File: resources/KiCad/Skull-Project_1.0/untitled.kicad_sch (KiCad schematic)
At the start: 1 part

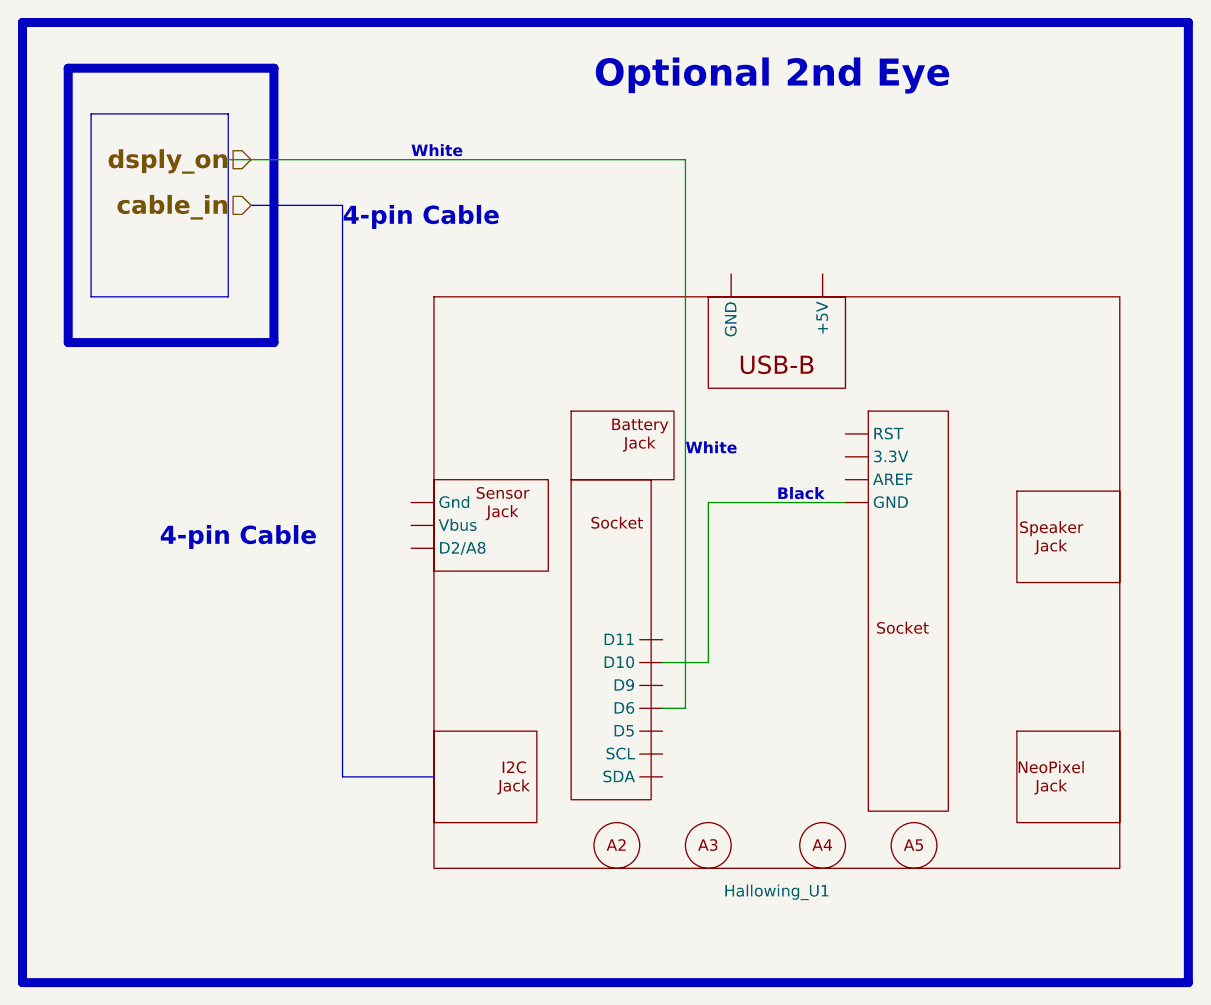
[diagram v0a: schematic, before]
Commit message: add rst-2-prim to schematic
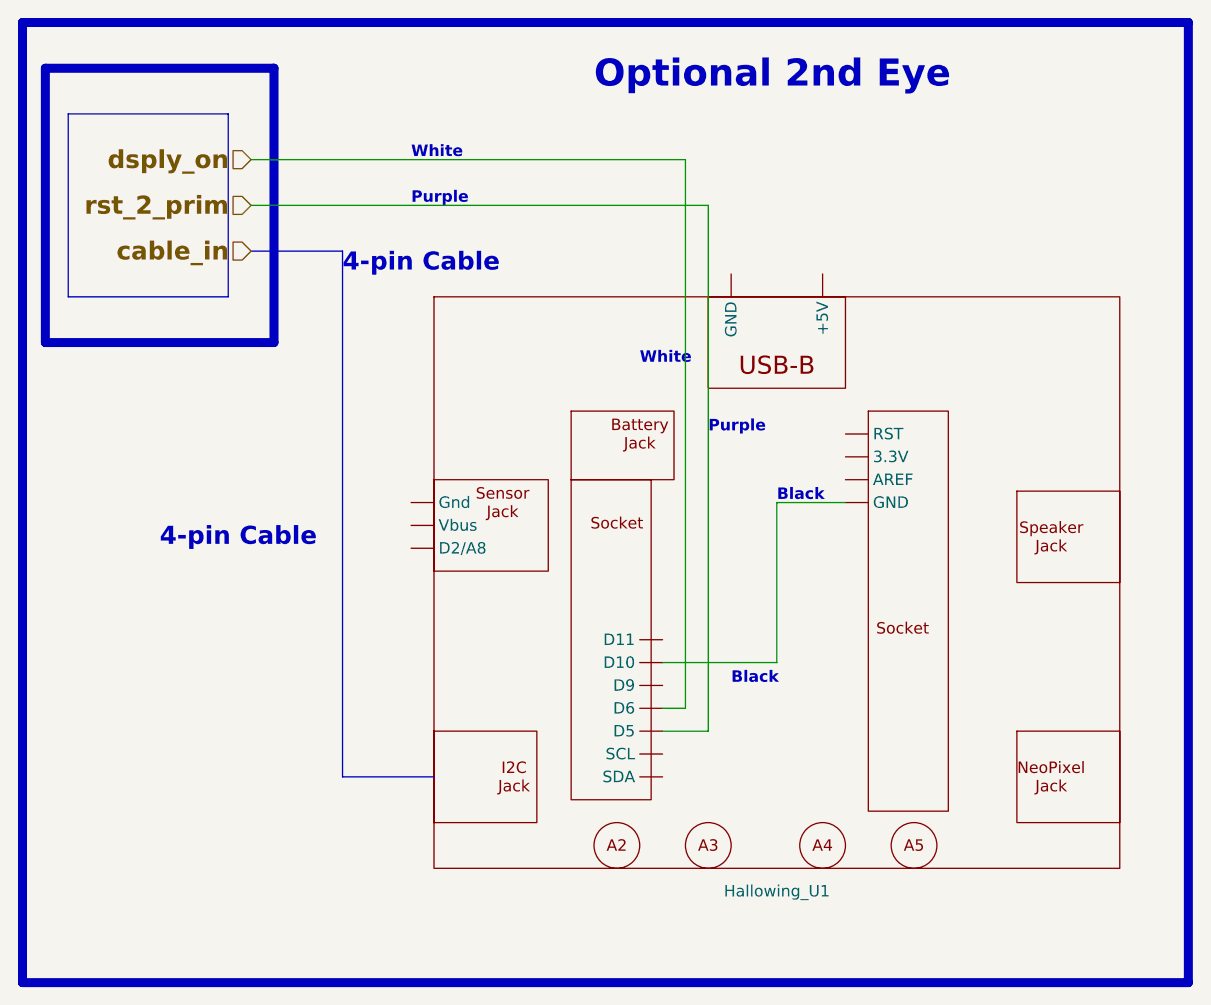
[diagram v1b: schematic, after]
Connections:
- net rst_2_prim : now reaches Hallowing_U1. (Vbus)
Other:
- note added: "Purple"
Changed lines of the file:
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@@
   (title_block
     (title "Skull-Project 1.0")
-    (date "2024-09-25")
+    (date "2024-09-27")
     (rev "1.0")
     (company "github.com/Mark-MDO47/Skull-Project")
     (comment 2 "NOTE: Hallowing as from display side (not connector side)")
   )
-  (wire (pts (xy 152.4 116.84) (xy 147.32 116.84))
+  (bus (pts (xy 101.6 71.12) (xy 111.76 71.12))
     (stroke (width 0) (type default))
   )
-  (bus (pts (xy 111.76 66.04) (xy 111.76 129.54))
+  (wire (pts (xy 101.6 60.96) (xy 149.86 60.96))
     (stroke (width 0) (type default))
   )
-  (wire (pts (xy 167.64 99.06) (xy 152.4 99.06))
+  (wire (pts (xy 147.32 116.84) (xy 160.02 116.84))
+    (stroke (width 0) (type default))
+  )
+  (wire (pts (xy 147.32 124.46) (xy 152.4 124.46))
+    (stroke (width 0) (type default))
+  )
+  (wire (pts (xy 167.64 99.06) (xy 160.02 99.06))
     (stroke (width 0) (type default))
   )
@@
     (stroke (width 0) (type default))
   )
-  (bus (pts (xy 101.6 66.04) (xy 111.76 66.04))
+  (wire (pts (xy 152.4 124.46) (xy 152.4 66.04))
+    (stroke (width 0) (type default))
+  )
+  (bus (pts (xy 111.76 71.12) (xy 111.76 129.54))
     (stroke (width 0) (type default))
   )
@@
     (stroke (width 0) (type default))
   )
-  (wire (pts (xy 99.06 60.96) (xy 149.86 60.96))
+  (wire (pts (xy 160.02 116.84) (xy 160.02 99.06))
     (stroke (width 0) (type default))
   )
-  (wire (pts (xy 152.4 99.06) (xy 152.4 116.84))
+  (wire (pts (xy 152.4 66.04) (xy 101.6 66.04))
     (stroke (width 0) (type default))
   )
@@
     (stroke (width 0) (type default))
   )
-  (rectangle (start 81.28 50.8) (end 104.14 81.28)
+  (rectangle (start 78.74 50.8) (end 104.14 81.28)
     (stroke (width 1) (type default) (color 255 153 0 1))
     (fill (type none))
   )
-  (rectangle (start 83.82 55.88) (end 99.06 76.2)
+  (rectangle (start 81.28 55.88) (end 99.06 76.2)
     (stroke (width 0) (type default))
     (fill (type none))
@@
     (fill (type none))
   )
+  (text "Black" (at 154.94 119.38 0)
+    (effects (font (size 1.27 1.27) bold) (justify left bottom))
+  )
   (text "Black" (at 160.02 99.06 0)
+    (effects (font (size 1.27 1.27) bold) (justify left bottom))
+  )
+  (text "Purple" (at 152.4 91.44 0)
     (effects (font (size 1.27 1.27) bold) (justify left bottom))
   )
@@
     (effects (font (size 1.27 1.27) bold) (justify left bottom))
   )
-  (text "4-pin Cable" (at 111.76 68.58 0)
+  (text "4-pin Cable" (at 111.76 73.66 0)
     (effects (font (size 2 2) bold) (justify left bottom))
+  )
+  (text "Purple" (at 119.38 66.04 0)
+    (effects (font (size 1.27 1.27) bold) (justify left bottom))
   )
   (text "4-pin Cable" (at 91.44 104.14 0)
@@
     (effects (font (size 3 3) (thickness 0.6) bold) (justify left bottom))
   )
-  (text "White" (at 149.86 93.98 0)
+  (text "White" (at 144.78 83.82 0)
     (effects (font (size 1.27 1.27) bold) (justify left bottom))
+  )
+  (hierarchical_label "rst_2_prim " (shape input) (at 101.6 66.04 180) (fields_autoplaced)
+    (effects (font (size 2 2) (thickness 0.4) bold) (justify right))
   )
   (hierarchical_label "dsply_on " (shape input) (at 101.6 60.96 180) (fields_autoplaced)
     (effects (font (size 2 2) bold) (justify right))
   )
-  (hierarchical_label "cable_in " (shape input) (at 101.6 66.04 180) (fields_autoplaced)
+  (hierarchical_label "cable_in " (shape input) (at 101.6 71.12 180) (fields_autoplaced)
     (effects (font (size 2 2) bold) (justify right))
   )
